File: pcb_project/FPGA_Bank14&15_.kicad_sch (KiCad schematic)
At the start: 18 parts, among them IC3 IS61WV204816BLL-10TLI, U7 XC7A100T-FTG256, U8 MT25QL128ABA1ESE-0SIT

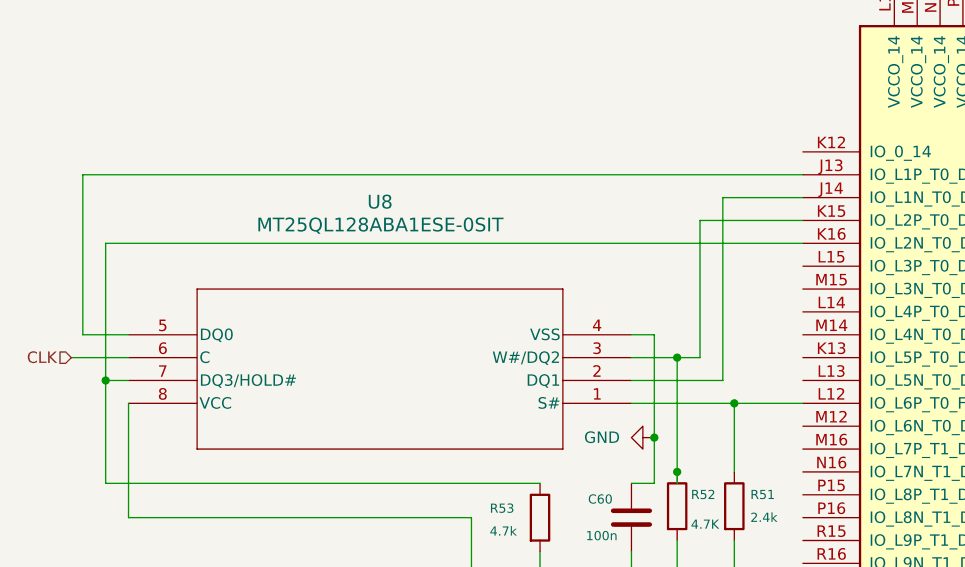
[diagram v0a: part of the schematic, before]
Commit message: Fix flash memory clk wiring
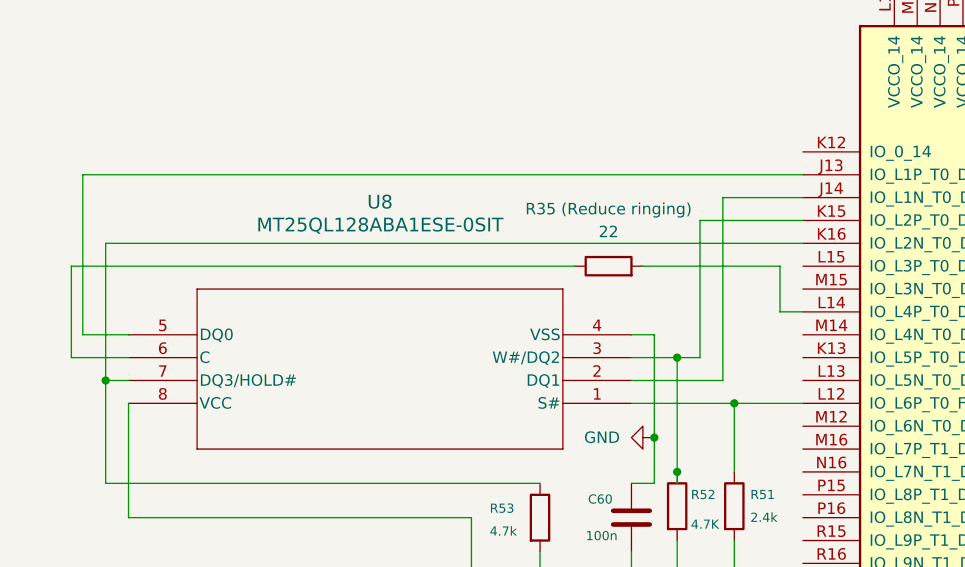
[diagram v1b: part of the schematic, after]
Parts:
- added R35 (Reduce ringing): 22, symbol Device:R
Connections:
- net at U7.L14 (IO_L4P_T0_D04_14): now also R35 (Reduce ringing).2
- net CLK: no longer names the net of U8.6 (C)
- net CLK: now also R35 (Reduce ringing).1
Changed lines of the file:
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@@
+	(wire
+		(pts
+			(xy 96.52 53.34) (xy 99.06 53.34)
+		)
+		(stroke
+			(width 0)
+			(type default)
+		)
+	)
 	(wire
 		(pts
@@
 	(wire
 		(pts
+			(xy 96.52 48.26) (xy 96.52 53.34)
+		)
+		(stroke
+			(width 0)
+			(type default)
+		)
+	)
+	(wire
+		(pts
 			(xy 248.92 115.57) (xy 251.46 115.57)
 		)
@@
 	(wire
 		(pts
+			(xy 17.78 48.26) (xy 73.66 48.26)
+		)
+		(stroke
+			(width 0)
+			(type default)
+		)
+	)
+	(wire
+		(pts
 			(xy 262.89 27.94) (xy 262.89 74.93)
 		)
@@
 	(wire
 		(pts
+			(xy 81.28 48.26) (xy 96.52 48.26)
+		)
+		(stroke
+			(width 0)
+			(type default)
+		)
+	)
+	(wire
+		(pts
 			(xy 250.19 118.11) (xy 250.19 124.46)
 		)
@@
 		(pts
 			(xy 172.72 73.66) (xy 185.42 73.66)
+		)
+		(stroke
+			(width 0)
+			(type default)
+		)
+	)
+	(wire
+		(pts
+			(xy 17.78 58.42) (xy 17.78 48.26)
 		)
 		(stroke
@@
 		(shape input)
 		(at 99.06 137.16 180)
-		(effects
-			(font
-				(size 1.27 1.27)
-			)
-			(justify right)
-		)
-	)
-	(hierarchical_label "CLK"
-		(shape input)
-		(at 17.78 58.42 180)
 		(effects
 			(font
@@
 					(unit 1)
 				)
+			)
+		)
+	)
+	(symbol
+		(lib_id "Device:R")
+		(at 77.47 48.26 90)
+		(unit 1)
+		(exclude_from_sim no)
+		(in_bom yes)
+		(on_board yes)
+		(dnp no)
+		(fields_autoplaced yes)
+		(property "Reference" "R35 (Reduce ringing)"
+			(at 77.47 41.91 90)
+			(effects
+				(font
+					(size 1.27 1.27)
+				)
+			)
+		)
+		(property "Value" "22"
+			(at 77.47 44.45 90)
+			(effects
+				(font
+					(size 1.27 1.27)
+				)
+			)
+		)
+		(property "Footprint" ""
+			(at 77.47 50.038 90)
+			(effects
+				(font
+					(size 1.27 1.27)
+				)
+				(hide yes)
+			)
+		)
+		(property "Datasheet" "~"
+			(at 77.47 48.26 0)
+			(effects
+				(font
+					(size 1.27 1.27)
+				)
+				(hide yes)
+			)
+		)
+		(property "Description" "Resistor"
+			(at 77.47 48.26 0)
+			(effects
+				(font
+					(size 1.27 1.27)
+				)
+				(hide yes)
+			)
+		)
+		(pin "2"
+		)
+		(pin "1"
+		)
+		(instances
+			(project ""
+				(path "/98f80f66-4595-4d0f-90ca-59b2db6f447b/8bdc4eb6-105b-4ccb-b86f-5b5221dfef47/6eb3ac2c-fa04-4536-9a86-3231e0211a3c"
+					(reference "R35 (Reduce ringing)")
+					(unit 1)
+				)

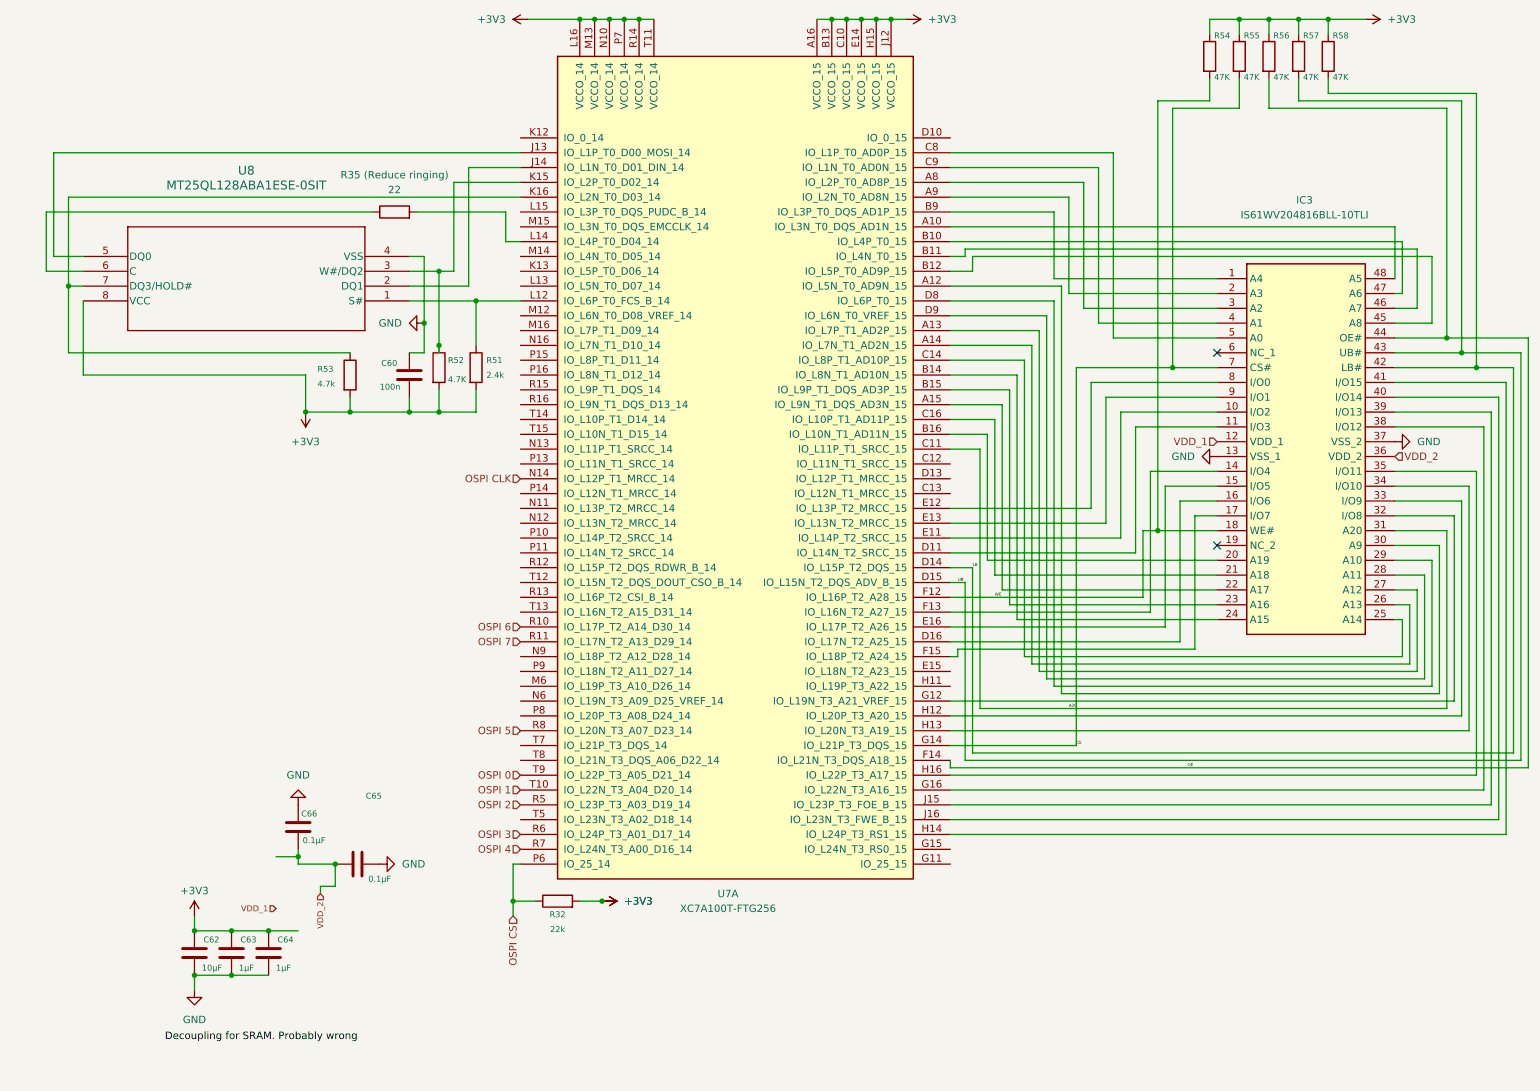
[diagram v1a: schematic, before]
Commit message: Add FPGA configuration LED's, config pins, no connect symbols
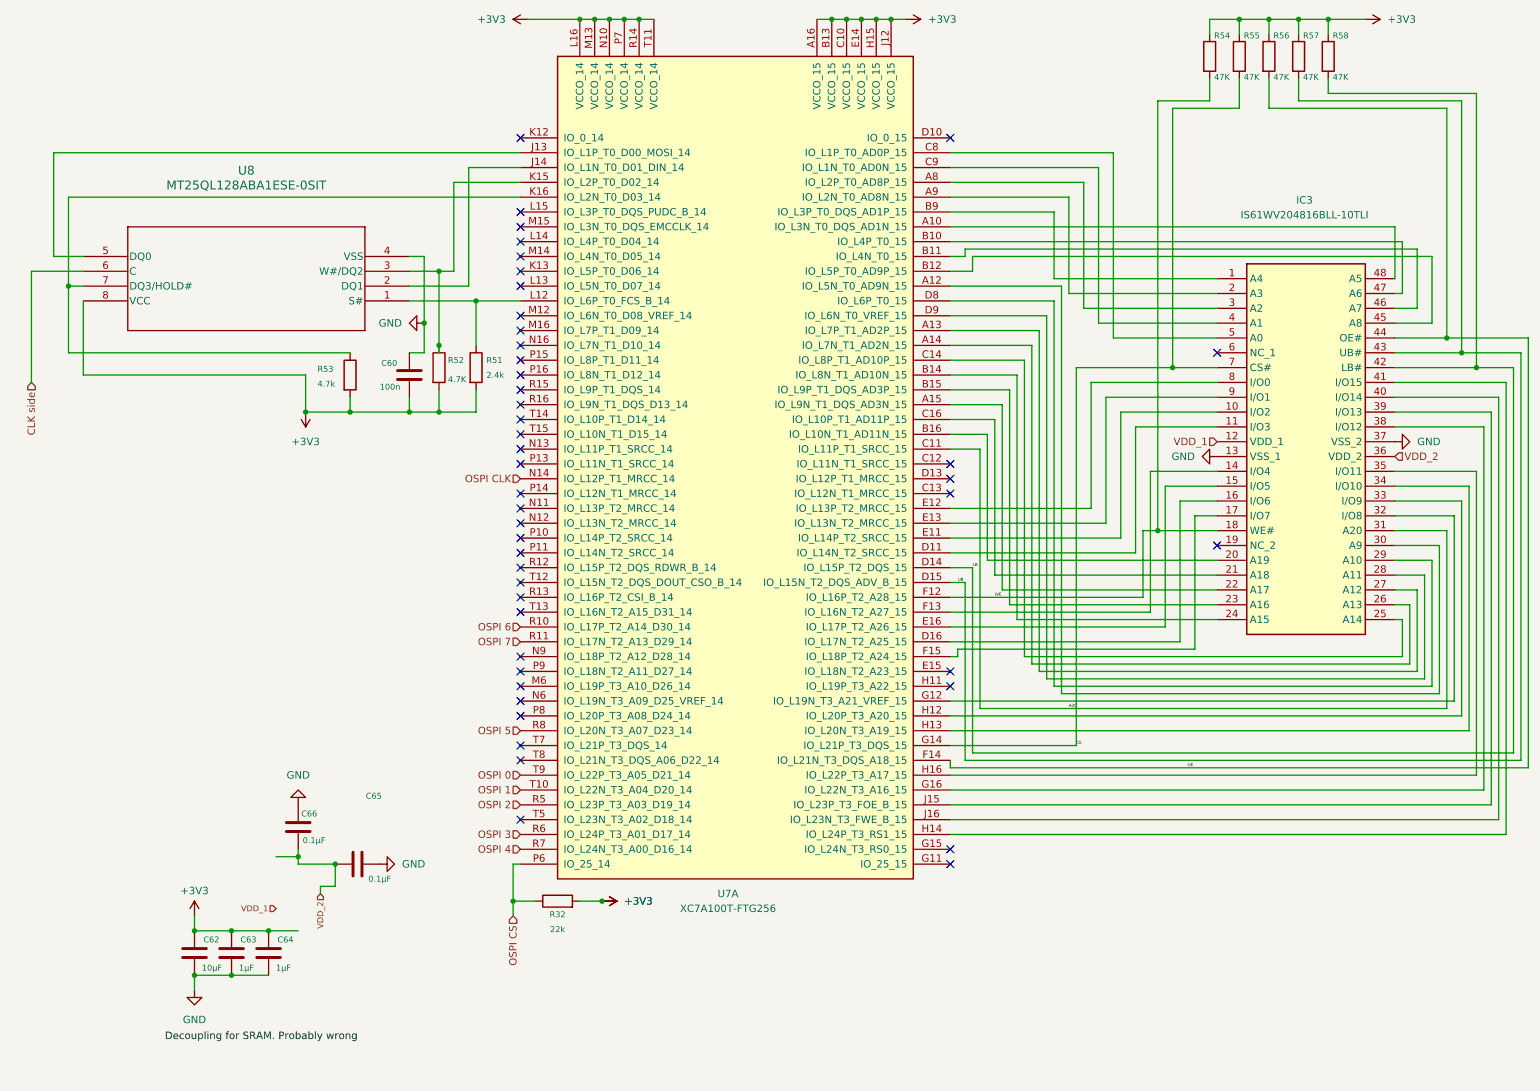
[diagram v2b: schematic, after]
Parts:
- removed R35 (Reduce ringing): 22, symbol Device:R
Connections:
- net CLK side: now reaches U8.6 (C)
- no-connect marks 2 -> 45

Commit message: ERC fixes, some remain
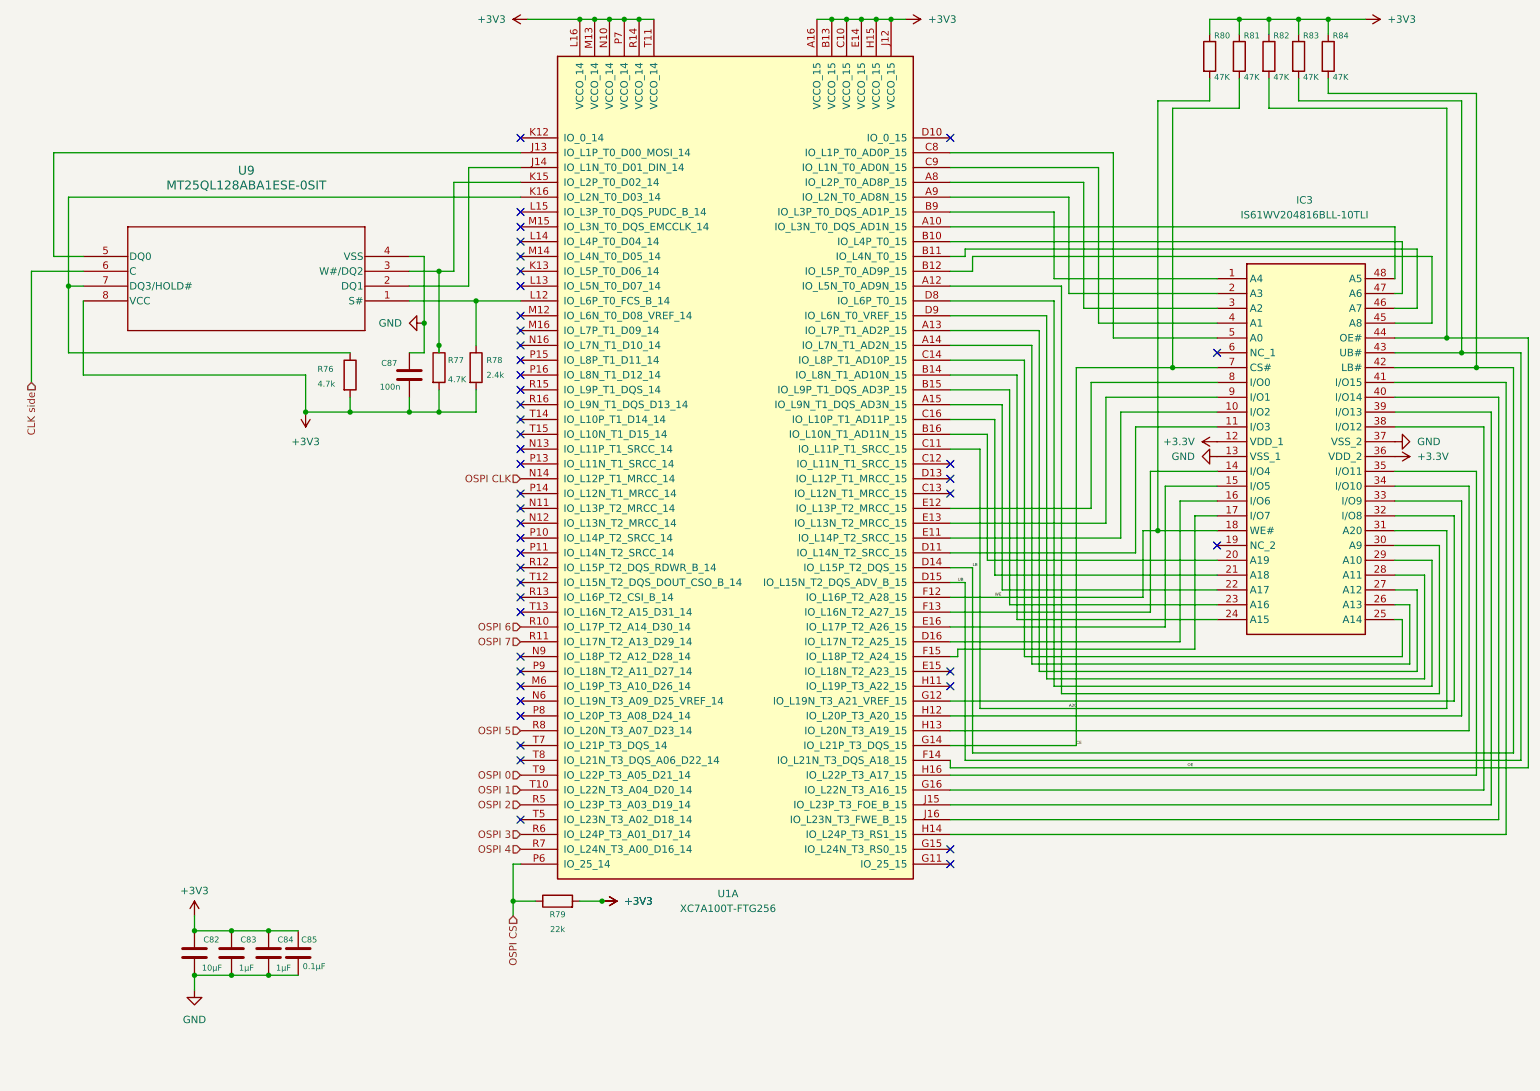
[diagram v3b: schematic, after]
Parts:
- removed C65: 0.1µF, symbol Device:C
- renumbered C62 to C82, C63 to C83, C64 to C84, C66 to C85, C60 to C87, R53 to R76, R52 to R77, R51 to R78, R32 to R79, R54 to R80, R55 to R81, R56 to R82, R57 to R83, R58 to R84, U7 to U1, U8 to U9
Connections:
- net +3V3: now also C85.1
- net GND: now also C85.2; no longer C85.1
- net VDD_1 renamed +3.3V
- net +3.3V: now also IC3.36 (VDD_2)
- removed net VDD_2: C85.2, IC3.36 (VDD_2)
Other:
- moved on the sheet: C85

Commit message: Fix JTAG connector, add pullups (FPGA has internal pullups as well), add some capacitor footprints
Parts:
- IC3: footprint SOP50P2000X120-48N -> Project_Footprints:SOP50P2000X120-48N
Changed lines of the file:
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@@
 			)
 		)
-		(property "Footprint" "SOP50P2000X120-48N"
+		(property "Footprint" "Project_Footprints:SOP50P2000X120-48N"
 			(at 245.11 154.61 0)
 			(effects

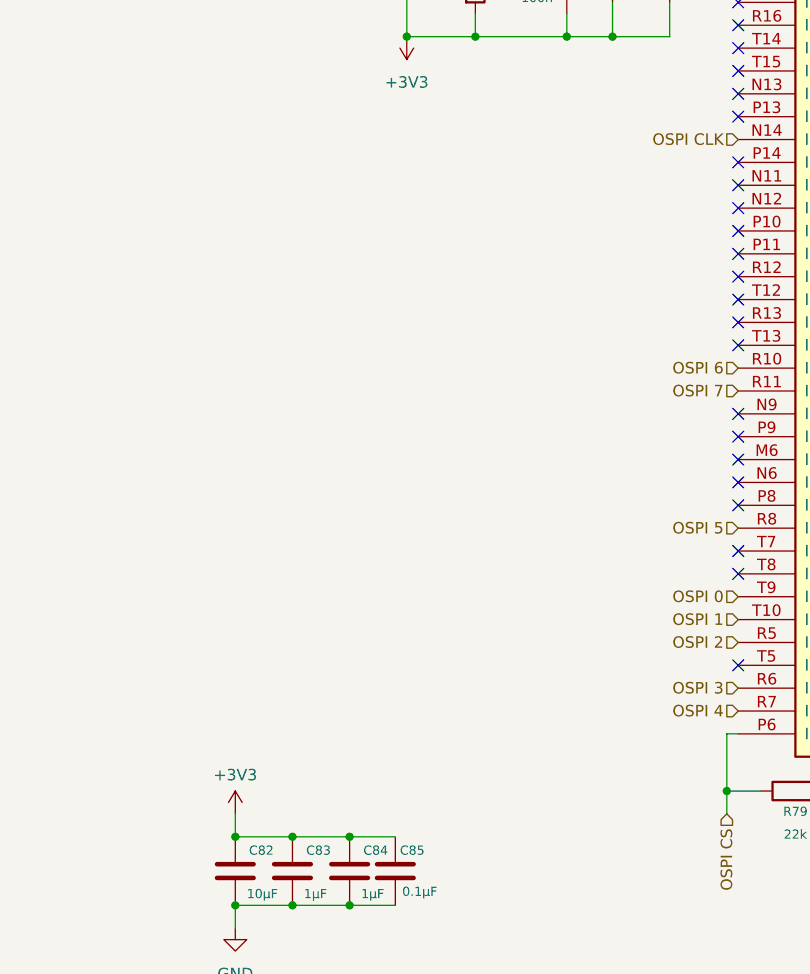
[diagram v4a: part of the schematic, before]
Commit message: Tied unused FGPA vcco to ground. Moved decoupling to all banks.
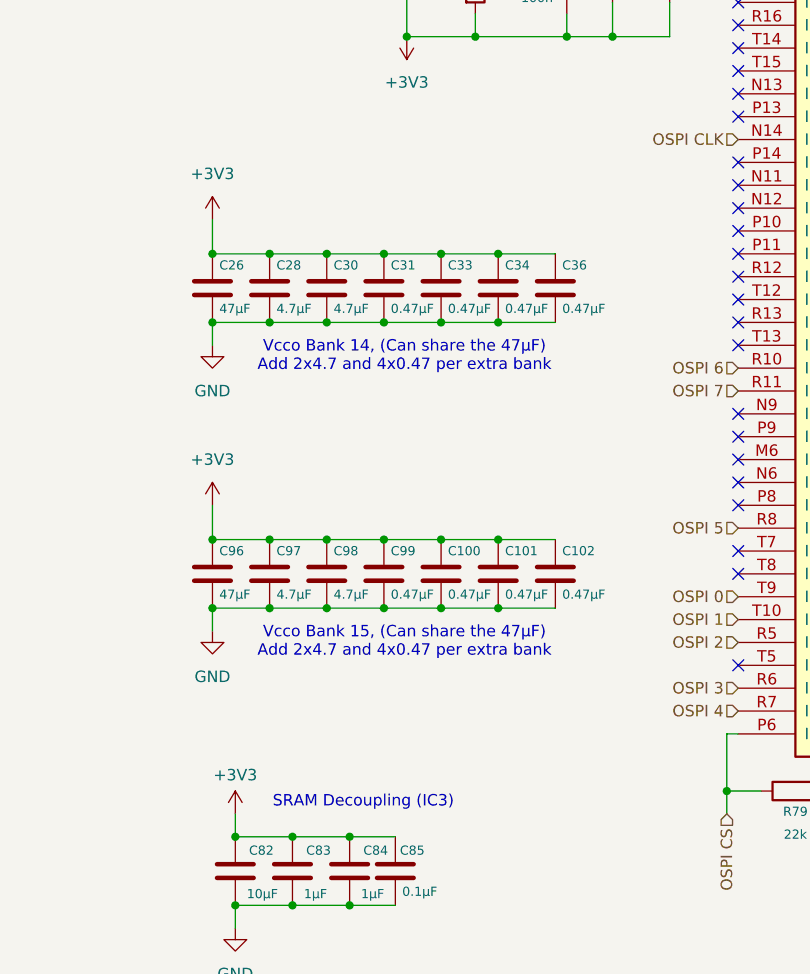
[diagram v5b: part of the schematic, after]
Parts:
- added C100, C101, C102, C31, C33, C34, C36, C99: 0.47µF, Capacitor_SMD:C_0805_2012Metric_Pad1.18x1.45mm_HandSolder, symbol Device:C
- added C26, C96: 47µF, Capacitor_SMD:C_1210_3225Metric_Pad1.33x2.70mm_HandSolder, symbol Device:C
- added C28, C30, C97, C98: 4.7µF, Capacitor_SMD:C_0805_2012Metric_Pad1.18x1.45mm_HandSolder, symbol Device:C
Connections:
- net +3V3: now also C100.1, C101.1, C102.1, C26.1, C28.1, C30.1, C31.1, C33.1, C34.1, C36.1, C96.1, C97.1, C98.1, C99.1
- net GND: now also C100.2, C101.2, C102.2, C26.2, C28.2, C30.2, C31.2, C33.2, C34.2, C36.2, C96.2, C97.2, C98.2, C99.2
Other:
- note added: "SRAM Decoupling (IC3)"
- note added: "Vcco Bank 14, (Can share the 47µF) Add 2x4.7 and 4x0.47 per extra bank"
- note added: "Vcco Bank 15, (Can share the 47µF) Add 2x4.7 and 4x0.47 per extra bank"
